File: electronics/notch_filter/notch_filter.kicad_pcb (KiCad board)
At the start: 2 copper layers, 2 parts

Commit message: further layout and placing
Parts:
- added C1: 1uF, SquantorRcl:C_0805+0603, B.Cu at (92.7, 68.4)
- added J1: Conn_01x02, Connector_JST:JST_PH_B2B-PH-K_1x02_P2.00mm_Vertical, F.Cu at (74.7, 74.1)
- added J2: Conn_01x02, Connector_JST:JST_PH_B2B-PH-K_1x02_P2.00mm_Vertical, F.Cu at (69.2, 74.1)
- added J3: Output, SquantorConnectors:Conn_BNC_RightAngle_TH, F.Cu at (87.5, 84.4)
- added J4: In, SquantorConnectors:Conn_BNC_RightAngle_TH, F.Cu at (72.5, 84.4)
- added J5: module_2x15_left_input, Connector_PinHeader_2.54mm:PinHeader_2x15_P2.54mm_Vertical, F.Cu at (61.0, 49.5)
- added J6: module_2x15_right_input, Connector_PinHeader_2.54mm:PinHeader_2x15_P2.54mm_Vertical, F.Cu at (96.5, 49.5)
- added J7: Conn_01x02, Connector_JST:JST_PH_B2B-PH-K_1x02_P2.00mm_Vertical, F.Cu at (88.7, 50.1)
- added J8: Conn_01x02, Connector_JST:JST_PH_B2B-PH-K_1x02_P2.00mm_Vertical, F.Cu at (88.7, 55.8)
- added R1: 10K, SquantorRcl:R_0805+0603, B.Cu at (84.1, 66.0)
- added R2: 10K, SquantorRcl:R_0805+0603, B.Cu at (84.1, 69.2)
- added R3: 1.2K, SquantorRcl:R_0805+0603, B.Cu at (93.1, 79.5)
- added R4: 1.2K, SquantorRcl:R_0805+0603, B.Cu at (93.1, 77.6)
- added U1: opamp_single_8pin, SquantorIC:SOIC-8-HAND, B.Cu at (88.7, 68.4)
- N1: value 20220506 -> 20230414
- moved N1 65.3 mm to (79.7, 62.3)
- moved N2 65.3 mm to (80.3, 58.4)
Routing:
- added copper zone on B.Cu, net GND
- added copper zone on F.Cu, net GND
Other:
- board outline added: 42.4 x 46.2 mm

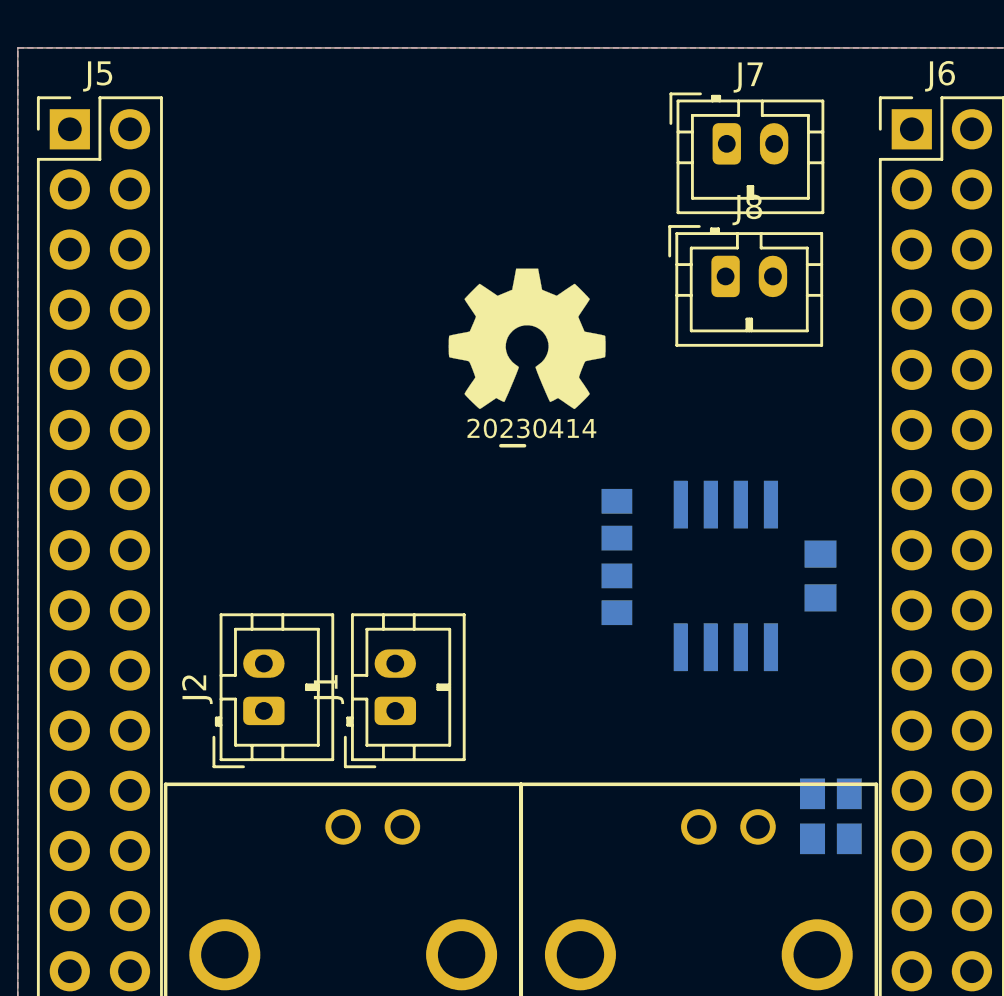
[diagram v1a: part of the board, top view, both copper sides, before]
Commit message: added filter and attenuator to schematic and placed components
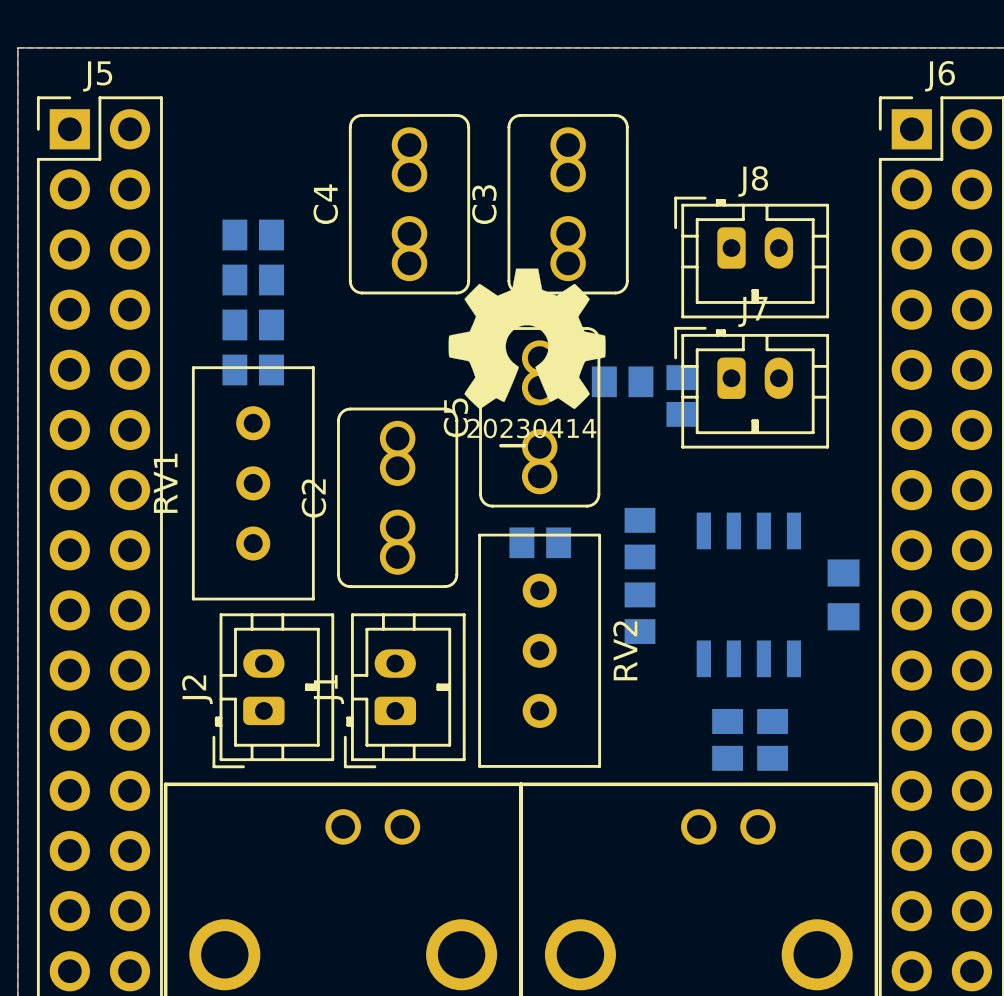
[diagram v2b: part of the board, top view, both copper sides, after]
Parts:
- added C2: 10n, SquantorRcl:C-025_050-050X100-film, F.Cu at (74.8, 65.1)
- added C3: 10n, SquantorRcl:C-025_050-050X100-film, F.Cu at (82.0, 52.7)
- added C4: 10n, SquantorRcl:C-025_050-050X100-film, F.Cu at (75.3, 52.7)
- added C5: 10n, SquantorRcl:C-025_050-050X100-film, F.Cu at (80.8, 61.7)
- added R10: 270, SquantorRcl:R_0805+0603, B.Cu at (68.7, 55.9)
- added R11: 7K68, SquantorRcl:R_0805+0603, B.Cu at (68.7, 54.0)
- added R5: 33K, SquantorRcl:R_0805+0603, B.Cu at (84.3, 60.2)
- added R6: 10, SquantorRcl:R_0805+0603, B.Cu at (86.8, 60.8)
- added R7: 100, SquantorRcl:R_0805+0603, B.Cu at (68.7, 59.7)
- added R8: 7K68, SquantorRcl:R_0805+0603, B.Cu at (68.7, 57.8)
- added R9: 3K9, SquantorRcl:R_0805+0603, B.Cu at (80.8, 67.0)
- added RV1: 200, Potentiometer_THT:Potentiometer_Bourns_3296W_Vertical, F.Cu at (68.7, 62.0)
- added RV2: 200, Potentiometer_THT:Potentiometer_Bourns_3296W_Vertical, F.Cu at (80.8, 74.1)
- U1: footprint SquantorIC:SOIC-8-HAND -> SquantorIC:SOIC-8
- moved J7 9.90 mm to (88.9, 60.0)
- moved R4 4.92 mm to (88.7, 75.3), turned to 90 degrees
- moved R3 4.85 mm to (90.6, 75.3), turned to 90 degrees
- moved C1 1.26 mm to (93.6, 69.2)
- moved U1 1.26 mm to (89.6, 69.2)
- moved R1 1.26 mm to (85.0, 66.8)
- moved R2 1.26 mm to (85.0, 70.0)
- moved J8 1.23 mm to (88.9, 54.5)
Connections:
- net /Output renamed /OUTPUT
- J1 pad 2: /Att_out -> /ATT_IN
- J2 pad 2: /Filt_in -> /FILT_IN
- J7 pad 1: /Amp_out -> /ATT_OUT
- J8 pad 1: /Filt_out -> /FILT_OUT

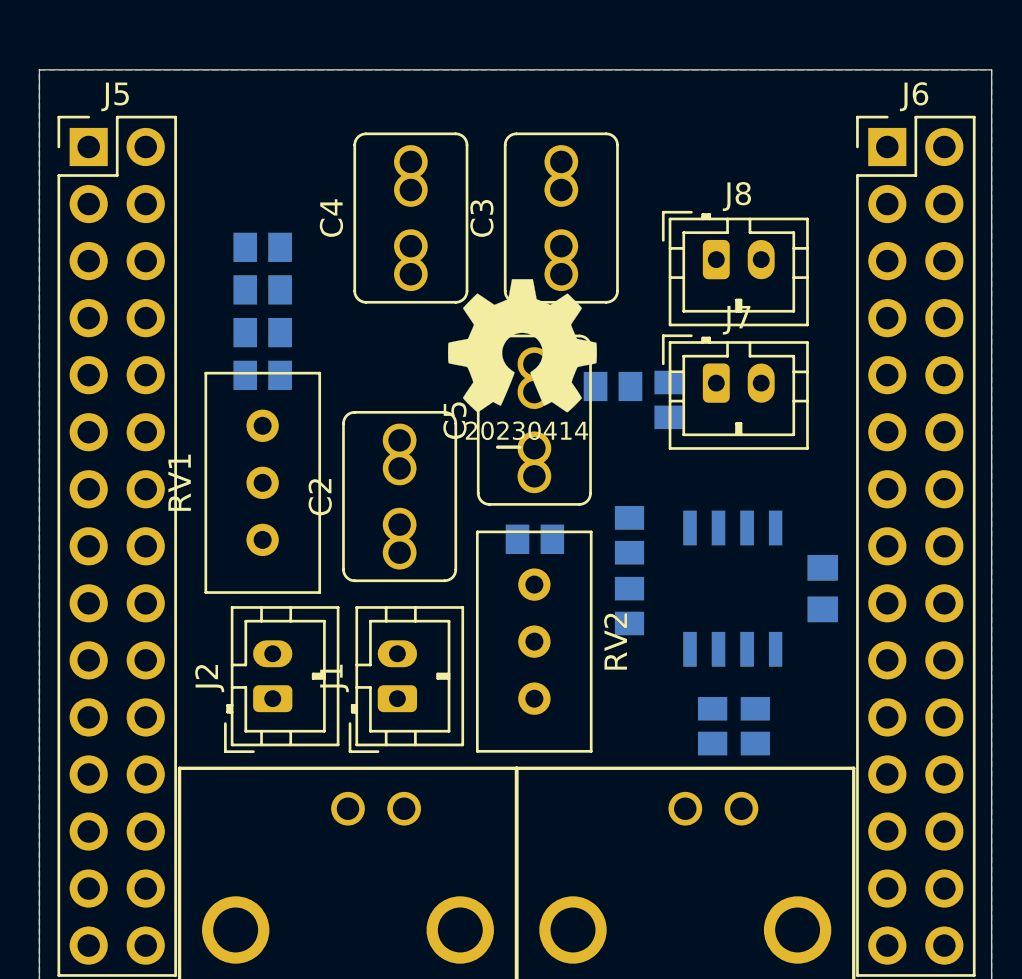
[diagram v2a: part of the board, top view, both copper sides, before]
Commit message: changed resistor networks to be more flexible, placed some components
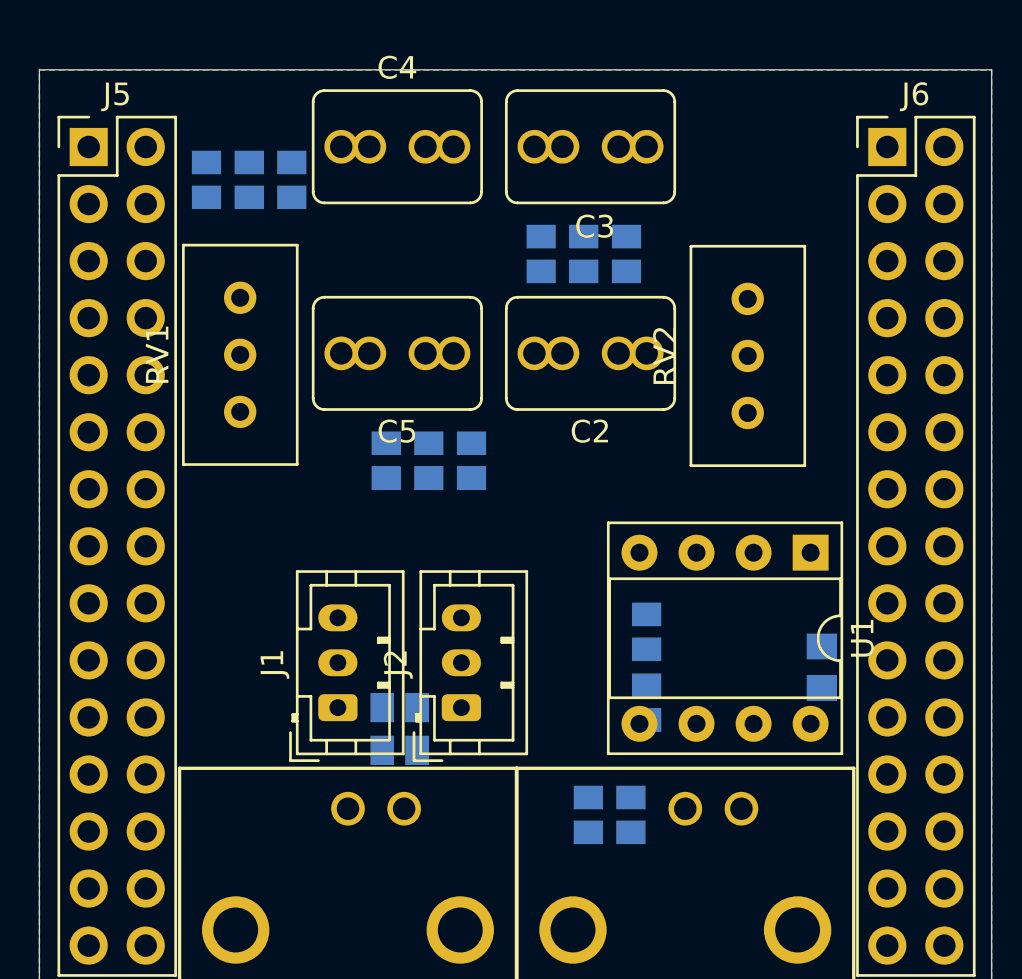
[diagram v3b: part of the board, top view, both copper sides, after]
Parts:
- removed J7, J8: Conn_01x02, Connector_JST:JST_PH_B2B-PH-K_1x02_P2.00mm_Vertical
- added R12: C/2, SquantorRcl:R_0805+0603, B.Cu at (76.1, 63.5)
- added R13: C, SquantorRcl:R_0805+0603, B.Cu at (66.2, 51.0)
- added R14: A/2, SquantorRcl:R_0805+0603, B.Cu at (78.0, 63.5)
- added R15: C, SquantorRcl:R_0805+0603, B.Cu at (81.1, 54.3)
- C2, C3, C4, C5: value 10n -> D
- J1, J2: value Conn_01x02 -> Conn_01x03; footprint Connector_JST:JST_PH_B2B-PH-K_1x02_P2.00mm_Vertical -> Connector_JST:JST_PH_B3B-PH-K_1x03_P2.00mm_Vertical
- N1, N2: moved to B.Cu
- R10: value 270 -> A
- R11, R8: value 7K68 -> B
- R7: value 100 -> A
- R9: value 3K9 -> B/2
- RV1, RV2: value 200 -> E
- U1: footprint SquantorIC:SOIC-8 -> Package_DIP:DIP-8_W7.62mm_Socket; moved to F.Cu
- moved N2 28.3 mm to (72.4, 85.6)
- moved N1 20.9 mm to (71.8, 81.7)
- moved RV2 20.2 mm to (90.3, 56.3), turned to 90 degrees
- moved R6 19.7 mm to (74.8, 76.4), turned to 0 degrees
- moved R5 17.2 mm to (74.8, 74.5)
- moved R10 16.3 mm to (84.9, 54.3), turned to 90 degrees
- moved R11 14.3 mm to (83.0, 54.3), turned to 90 degrees
- moved C2 10.6 mm to (83.3, 58.7), turned to 180 degrees
- moved R7 8.80 mm to (70.0, 51.0), turned to 90 degrees
- moved J2 8.41 mm to (77.5, 74.5)
- moved R9 7.49 mm to (74.2, 63.5), turned to -90 degrees
- moved R8 6.83 mm to (68.1, 51.0), turned to -90 degrees
- moved R3 6.80 mm to (85.1, 79.3)
- moved R4 6.80 mm to (83.2, 79.3)
- moved C5 6.79 mm to (74.7, 58.7), turned to 180 degrees
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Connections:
- J1 pad 1: Net-(J1-Pad1) -> /ATT_IN
- J1 pad 2: /ATT_IN -> Net-(J4-Pad1)
- J2 pad 1: Net-(J1-Pad1) -> /ATT_OUT
- J2 pad 2: /FILT_IN -> Net-(U1-Pad3)
- J4 pad 1: Net-(J1-Pad1) -> Net-(J4-Pad1)
- RV2 pad 3: Net-(R9-Pad1) -> Net-(RV2-Pad3)
- U1 pad 3: Net-(J7-Pad2) -> Net-(U1-Pad3)

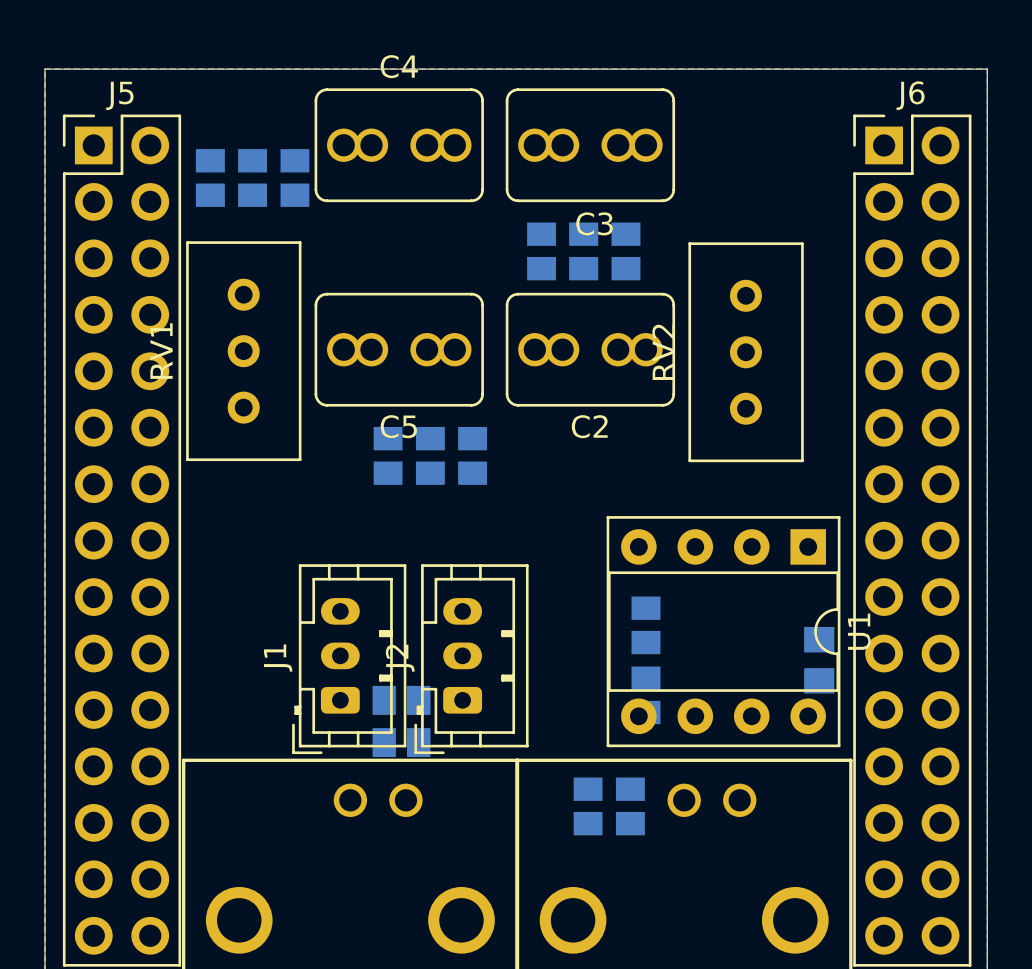
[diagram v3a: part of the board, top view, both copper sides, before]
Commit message: added compensation capacitor, placed and routed filter
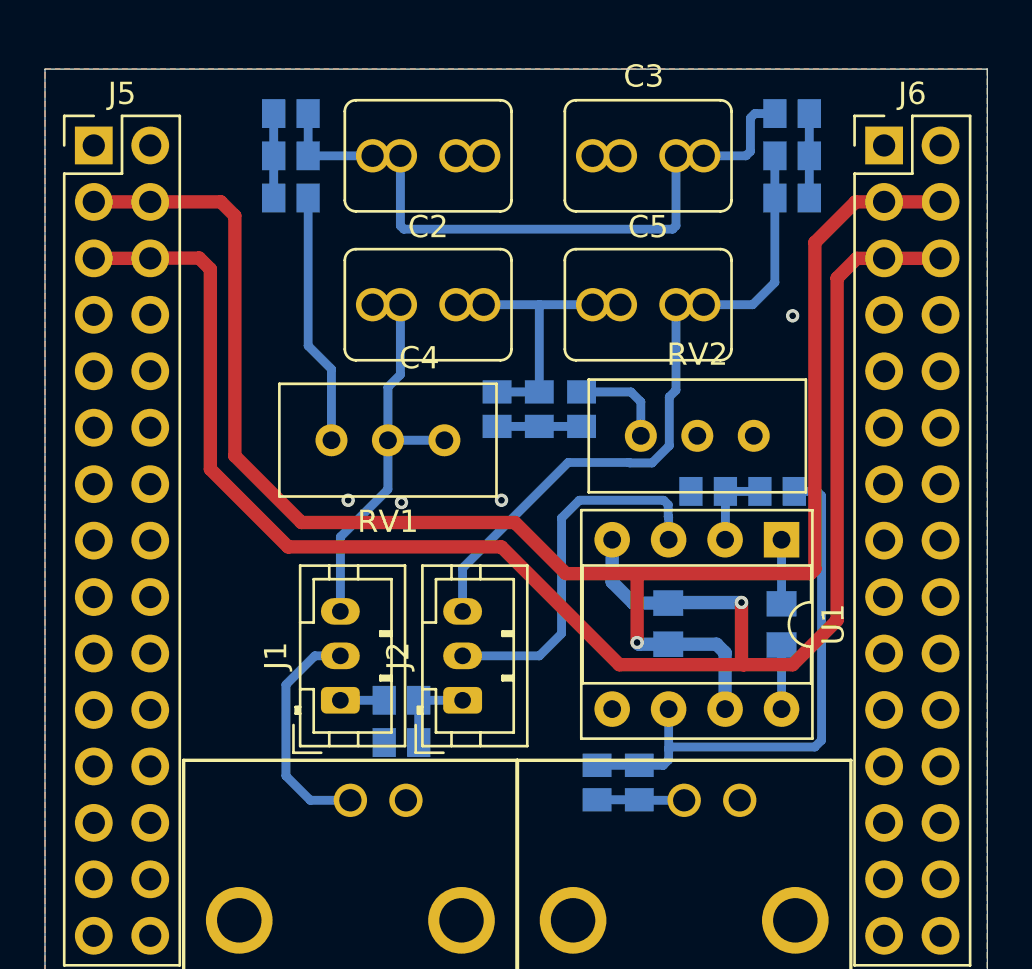
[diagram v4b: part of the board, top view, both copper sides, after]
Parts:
- added C6: compen, SquantorRcl:C_0805+0603, B.Cu at (91.9, 71.1)
- moved R15 11.5 mm to (92.4, 51.9), turned to 180 degrees
- moved C5 11.4 mm to (85.9, 56.7), turned to 0 degrees
- moved R2 10.9 mm to (91.7, 65.1), turned to 0 degrees
- moved R11 10.3 mm to (92.4, 50.0), turned to 180 degrees
- moved R10 9.71 mm to (92.4, 48.1), turned to 0 degrees
- moved RV1 7.65 mm to (71.7, 62.8), turned to 180 degrees
- moved C2 7.58 mm to (76.0, 56.7), turned to 0 degrees
- moved C1 7.00 mm to (86.8, 71.0)
- moved R1 6.64 mm to (88.6, 65.1), turned to 0 degrees
- moved RV2 6.31 mm to (90.7, 62.6), turned to 0 degrees
- moved R12 5.33 mm to (81.0, 61.4), turned to 90 degrees
- moved R14 5.33 mm to (82.9, 61.4)
- moved R9 5.33 mm to (79.1, 61.4), turned to 90 degrees
- moved R13 3.76 mm to (69.8, 50.0), turned to 0 degrees
- moved R8 3.37 mm to (69.8, 48.1), turned to 0 degrees
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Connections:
- U1 pad 1: unconnected-(U1-Pad1) -> Net-(U1-Pad1)
- U1 pad 8: unconnected-(U1-Pad8) -> Net-(U1-Pad8)
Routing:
- net -15V: track 0.00 -> 78.5 mm, vias 0 -> 1
- net +15V: track 0.00 -> 76.7 mm, vias 0 -> 1
- net /FILT_OUT: track 0.00 -> 29.3 mm
- net Net-(C3-Pad2): track 0.00 -> 28.5 mm
- net Net-(R2-Pad2): track 0.00 -> 25.0 mm
- net /FILT_IN: track 0.00 -> 17.5 mm
- net Net-(U1-Pad3): track 0.00 -> 16.9 mm
- net Net-(R7-Pad1): track 0.00 -> 11.3 mm
- net Net-(C2-Pad2): track 0.00 -> 10.7 mm
- net Net-(J4-Pad1): track 0.00 -> 10.4 mm
- net Net-(RV2-Pad3): track 0.00 -> 4.38 mm
- net /OUTPUT: track 0.00 -> 3.93 mm
- net /ATT_OUT: track 0.00 -> 3.88 mm
- net Net-(R9-Pad1): track 0.00 -> 3.80 mm
- net Net-(R7-Pad2): track 0.00 -> 3.80 mm
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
